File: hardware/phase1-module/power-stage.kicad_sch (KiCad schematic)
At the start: 0 parts

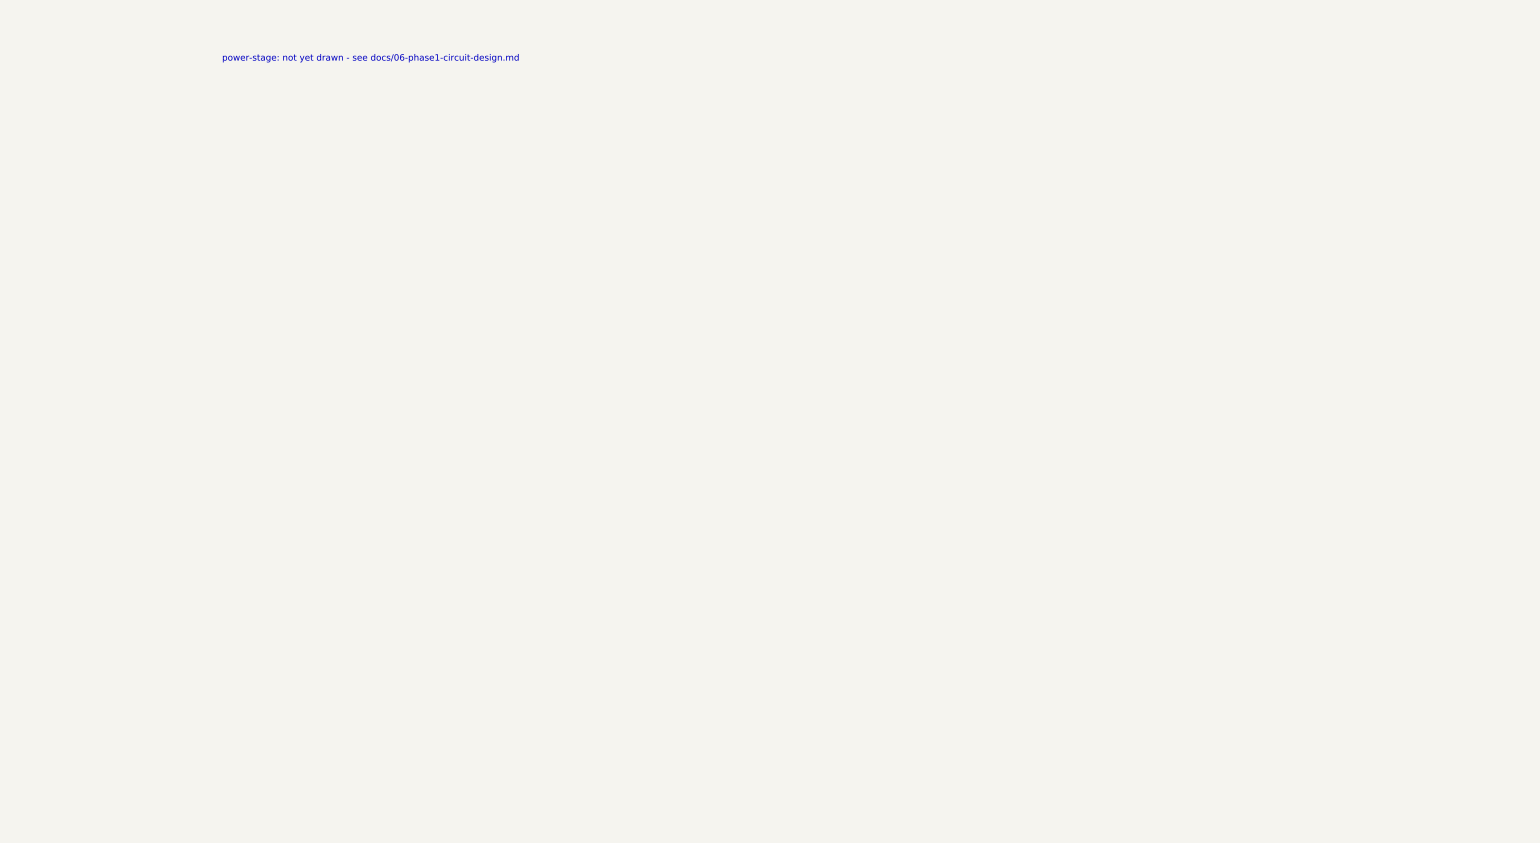
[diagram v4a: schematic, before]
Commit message: Complete Phase-1 schematic: all six remaining sheets, netlist-verified
- power-stage: LM5145 @350kHz (RT 28.7K per ds eq.3), RDS(on) valley
  ILIM 365R->SW, UVLO divider, EN kill chain (NOT(HW_EN) OR PS_OFF via
  Q5/Q6 + diode-OR), Type-III comp starting values, SYNCIN as DEM/FPWM
- sensing: 2m shunt, INA240A3 -> CC loop, INA228 telemetry, /8 divider,
  NT1 single AGND-PGND tie
- disconnect: back-to-back FETs + LTC7004, INP = OUT_REQ AND NOT(kill)
  AND NOT(OVP); TLV7011 + Q9 trips at 22.25V
- aux-rails: LMR36015 (5.016V) -> NCP1117 3V3
- mcu-can: STM32G431CBT6 fully pinned; I2C moved to I2C2/PA8-PA9 (PB8
  is the BOOT0 strap - pullup there would boot the ROM loader), BOOT0
  strapped low, OUT_REQ on PB14 (PB4 NJTRST reset pull-up), 8MHz
  crystal for CAN, TCAN1042 (VCC 5V, VIO 3V3)
- io: fused input + SMBJ33A TVS, output, backplane header, fan switch
  (1N4148W flyback orientation corrected: pin 1 = cathode)
- checker: duplicate-ref detection + global/local split-net detection;
  caught duplicate C62 and the LMR36015 FB-pin placement collision

Co-Authored-By: Claude Fable 5 <noreply@anthropic.com>
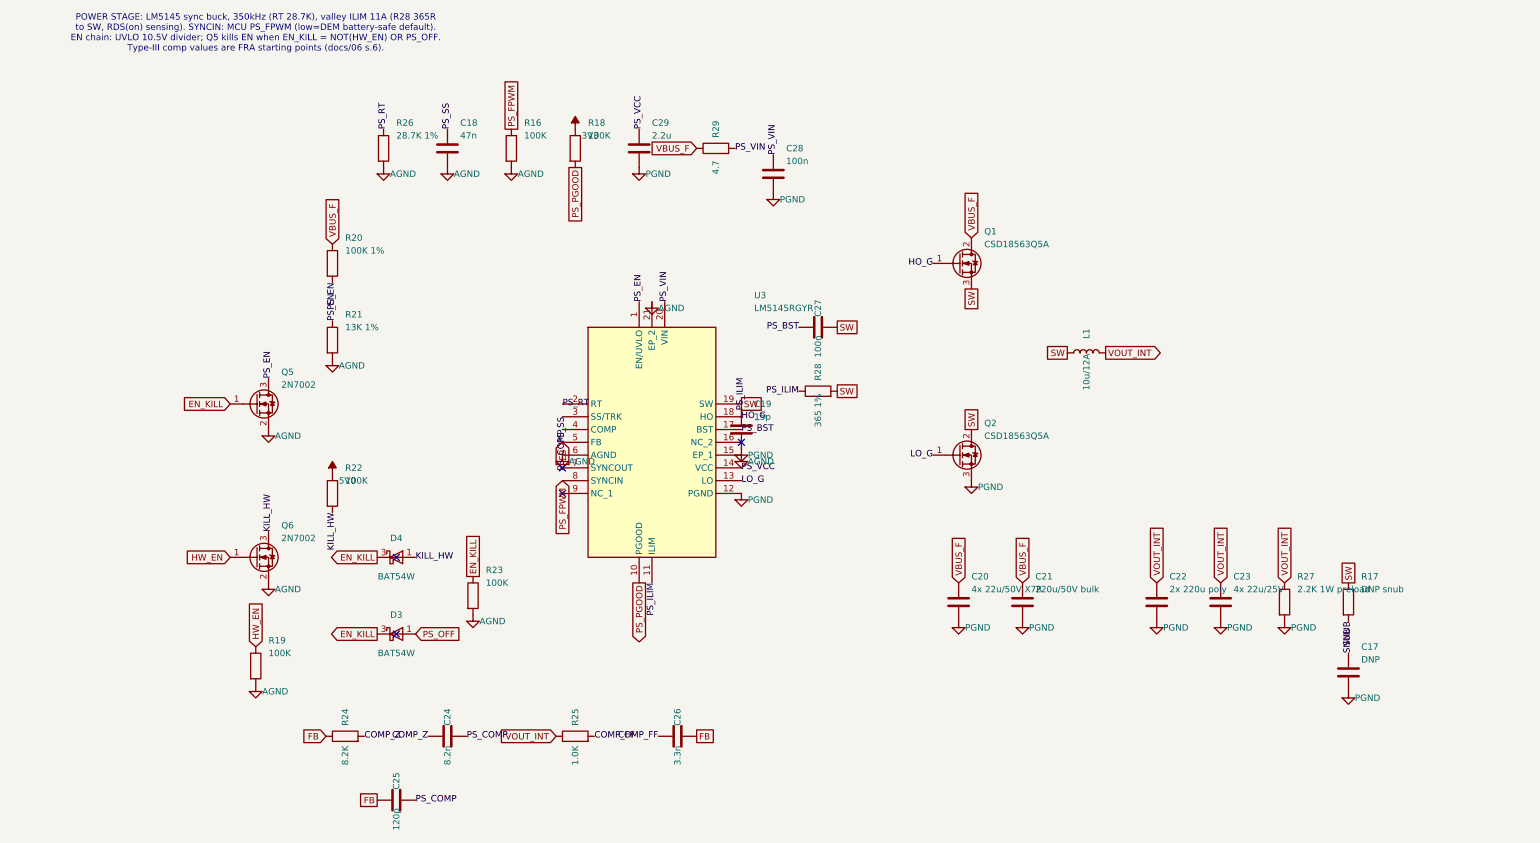
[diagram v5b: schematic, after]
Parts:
- added C17: DNP, Capacitor_SMD:C_0402_1005Metric, symbol Device:C
- added C18: 47n, Capacitor_SMD:C_0402_1005Metric, symbol Device:C
- added C19: 15p, Capacitor_SMD:C_0402_1005Metric, symbol Device:C
- added C20: 4x 22u/50V X7R, Capacitor_SMD:C_1210_3225Metric, symbol Device:C
- added C21: 220u/50V bulk, Capacitor_SMD:C_1210_3225Metric, symbol Device:C
- added C22: 2x 220u poly, Capacitor_SMD:C_1210_3225Metric, symbol Device:C
- added C23: 4x 22u/25V, Capacitor_SMD:C_1210_3225Metric, symbol Device:C
- added C24: 8.2n, Capacitor_SMD:C_0402_1005Metric, symbol Device:C
- added C25: 120p, Capacitor_SMD:C_0402_1005Metric, symbol Device:C
- added C26: 3.3n, Capacitor_SMD:C_0402_1005Metric, symbol Device:C
- added C27, C28: 100n, Capacitor_SMD:C_0402_1005Metric, symbol Device:C
- added C29: 2.2u, Capacitor_SMD:C_0402_1005Metric, symbol Device:C
- added D3, D4: BAT54W, Package_TO_SOT_SMD:SOT-323_SC-70, symbol Diode:BAT54W
- added L1: 10u/12A, labbench:L_10uH_flatwire_13x13, symbol Device:L
- added Q1, Q2: CSD18563Q5A, labbench:PowerFET_5x6, symbol Device:Q_NMOS_GDS
- added Q5, Q6: 2N7002, Package_TO_SOT_SMD:SOT-23, symbol Transistor_FET:2N7002
- added R16, R18, R19, R22, R23: 100K, Resistor_SMD:R_0402_1005Metric, symbol Device:R
- added R17: DNP snub, Resistor_SMD:R_0402_1005Metric, symbol Device:R
- added R20: 100K 1%, Resistor_SMD:R_0402_1005Metric, symbol Device:R
- added R21: 13K 1%, Resistor_SMD:R_0402_1005Metric, symbol Device:R
- added R24: 8.2K, Resistor_SMD:R_0402_1005Metric, symbol Device:R
- added R25: 1.0K, Resistor_SMD:R_0402_1005Metric, symbol Device:R
- added R26: 28.7K 1%, Resistor_SMD:R_0402_1005Metric, symbol Device:R
- added R27: 2.2K 1W preload, Resistor_SMD:R_0402_1005Metric, symbol Device:R
- added R28: 365 1%, Resistor_SMD:R_0402_1005Metric, symbol Device:R
- added R29: 4.7, Resistor_SMD:R_0402_1005Metric, symbol Device:R
- added U3: LM5145RGYR, labbench:LM5145_RGY_VQFN-20, symbol labbench:LM5145RGYR
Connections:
- new net 3V3: R18.1
- new net 5V0: R22.1
- new net AGND: C18.2, Q5.2 (S), Q6.2 (S), R16.2, R19.2, R21.2, R23.2, R26.2, U3.15 (EP_1), U3.21 (EP_2), U3.6 (AGND)
- new net COMP_FF: C26.1, R25.2
- new net COMP_Z: C24.1, R24.2
- new net EN_KILL: D3.3 (K), D4.3 (K), Q5.1 (G), R23.1
- new net FB: C25.1, C26.2, R24.1, U3.5 (FB)
- new net HO_G: Q1.1 (G), U3.18 (HO)
- new net HW_EN: Q6.1 (G), R19.1
- new net KILL_HW: D4.1 (A), Q6.3 (D), R22.2
- new net LO_G: Q2.1 (G), U3.13 (LO)
- new net PGND: C17.2, C19.2, C20.2, C21.2, C22.2, C23.2, C28.2, C29.2, Q2.3 (S), R27.2, U3.12 (PGND)
- new net PS_BST: C27.1, U3.17 (BST)
- new net PS_COMP: C24.2, C25.2, U3.4 (COMP)
- new net PS_EN: Q5.3 (D), R20.2, R21.1, U3.1 (EN/UVLO)
- new net PS_FPWM: R16.1, U3.8 (SYNCIN)
- new net PS_ILIM: C19.1, R28.1, U3.11 (ILIM)
- new net PS_OFF: D3.1 (A)
- new net PS_PGOOD: R18.2, U3.10 (PGOOD)
- new net PS_RT: R26.1, U3.2 (RT)
- new net PS_SS: C18.1, U3.3 (SS/TRK)
- new net PS_VCC: C29.1, U3.14 (VCC)
- new net PS_VIN: C28.1, R29.2, U3.20 (VIN)
- new net SNUB: C17.1, R17.2
- new net SW: C27.2, L1.1, Q1.3 (S), Q2.2 (D), R17.1, R28.2, U3.19 (SW)
- new net VBUS_F: C20.1, C21.1, Q1.2 (D), R20.1, R29.1
- new net VOUT_INT: C22.1, C23.1, L1.2, R25.1, R27.1
- no-connect marks 0 -> 5
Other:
- note added: "POWER STAGE: LM5145 sync buck, 350kHz (RT 28.7K), valley ILIM 11A (R28 365R to SW, RDS(on) sensing). SYNCIN: MCU PS_FPWM (low=DEM battery-safe default). EN chain: UVLO 10.5V divider; Q5 kills EN when EN_KILL = NOT(HW_EN) OR PS_OFF. Type-III comp values are FRA starting points (docs/06 s.6)."
- note removed: "power-stage: not yet drawn - see docs/06-phase1-circuit-design.md"

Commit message: Footprint pass: labbench.pretty library, all 137 components verified
- build_fplib.py: merges vetted vendor footprints (LM5145 RGY0020B,
  LMR36015 RNX, DAC80502 WSON-10 no-EP) and generates PowerFET_SON5x6_GDS
  from the TI Q5A land pattern (CSD18563Q5A SLPS444C) with pads renumbered
  1=G/2=D/3=S to match the generic NMOS symbol; writes fp-lib-table.
- check_footprints.py: every component must have a resolvable footprint and
  every netted pin a matching pad (caught a wrong official VSSOP-8 name).
- gen_phase1.py: passives 0402->0603 (hand assembly); DAC80502 vendor fp
  (DRX has no exposed pad); L1 = Coilcraft XAL1350-103ME on official fp;
  net-tie fp; crystal -> Crystal_GND24 with grounded shield pads; bulk cap
  banks expanded to one component per physical cap (C75-C81); R27 preload
  1W -> 2512.
- PARTS-TO-DOWNLOAD.md section D: new orderables for the footprint pass.

check_netlist + check_footprints: all OK (137 components).

Co-Authored-By: Claude Fable 5 <noreply@anthropic.com>
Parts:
- removed C21: 220u/50V bulk, Capacitor_SMD:C_1210_3225Metric, symbol Device:C
- removed C22: 2x 220u poly, Capacitor_SMD:C_1210_3225Metric, symbol Device:C
- added C21: 220u/50V, Capacitor_SMD:CP_Elec_10x10.5, symbol Device:C_Polarized
- added C22, C78: 220u/25V poly, Capacitor_SMD:CP_Elec_8x11.9, symbol Device:C_Polarized
- added C75, C76, C77: 22u/50V X7R, Capacitor_SMD:C_1210_3225Metric, symbol Device:C
- added C79, C80, C81: 22u/25V X7R, Capacitor_SMD:C_1210_3225Metric, symbol Device:C
- C17, C18, C19, C24, C25, C26, C27, C28, C29: footprint Capacitor_SMD:C_0402_1005Metric -> Capacitor_SMD:C_0603_1608Metric
- C20: value 4x 22u/50V X7R -> 22u/50V X7R
- C23: value 4x 22u/25V -> 22u/25V X7R
- L1: value 10u/12A -> XAL1350-103ME 10u/14A; footprint labbench:L_10uH_flatwire_13x13 -> Inductor_SMD:L_Coilcraft_XAL1350-XXX
- Q1, Q2: footprint labbench:PowerFET_5x6 -> labbench:PowerFET_SON5x6_GDS
- R16, R17, R18, R19, R20, R21, R22, R23, R24, R25, R26, R28, R29: footprint Resistor_SMD:R_0402_1005Metric -> Resistor_SMD:R_0603_1608Metric
- R27: footprint Resistor_SMD:R_0402_1005Metric -> Resistor_SMD:R_2512_6332Metric
- U3: footprint labbench:LM5145_RGY_VQFN-20 -> labbench:LM5145_RGY0020B
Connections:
- net PGND: now also C21.2, C22.2, C75.2, C76.2, C77.2, C78.2, C79.2, C80.2, C81.2
- net VBUS_F: now also C21.1, C75.1, C76.1, C77.1
- net VOUT_INT: now also C22.1, C78.1, C79.1, C80.1, C81.1
